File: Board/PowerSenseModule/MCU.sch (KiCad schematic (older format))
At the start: 29 parts, among them J3 Programming Header, J4 Conn_01x02_Male, U2 NCV2007x, U3 dsPIC33EV32GM102, U4 MCP2542FDxMF

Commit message: Moses's changes, removed MPLAB proj
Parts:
- added D3, D4: LED, Resistor_SMD:R_0603_1608Metric_Pad1.05x0.95mm_HandSolder, symbol Device:LED
- added R20, R21: 300, Resistor_SMD:R_0603_1608Metric_Pad1.05x0.95mm_HandSolder, symbol Device:R_US
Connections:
- net labels removed: +3.3V
- wire segments 122 -> 159
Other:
- note added: "Green"
- note added: "Red\n"
- moved on the sheet: C12

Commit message: BASE/REFERENCE
Initial Design.
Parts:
- J4: footprint Connector_PinHeader_2.54mm:PinHeader_1x02_P2.54mm_Vertical_SMD_Pin1Left -> Connector_PinHeader_2.54mm:PinHeader_1x02_P2.54mm_Vertical
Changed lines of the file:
@@
 F 0 "J4" H 1008 6206 50  0000 C CNN
 F 1 "Conn_01x02_Male" H 1008 6115 50  0000 C CNN
-F 2 "Connector_PinHeader_2.54mm:PinHeader_1x02_P2.54mm_Vertical_SMD_Pin1Left" H 900 6025 50  0001 C CNN
+F 2 "Connector_PinHeader_2.54mm:PinHeader_1x02_P2.54mm_Vertical" H 900 6025 50  0001 C CNN
 F 3 "~" H 900 6025 50  0001 C CNN
 	1    900  6025

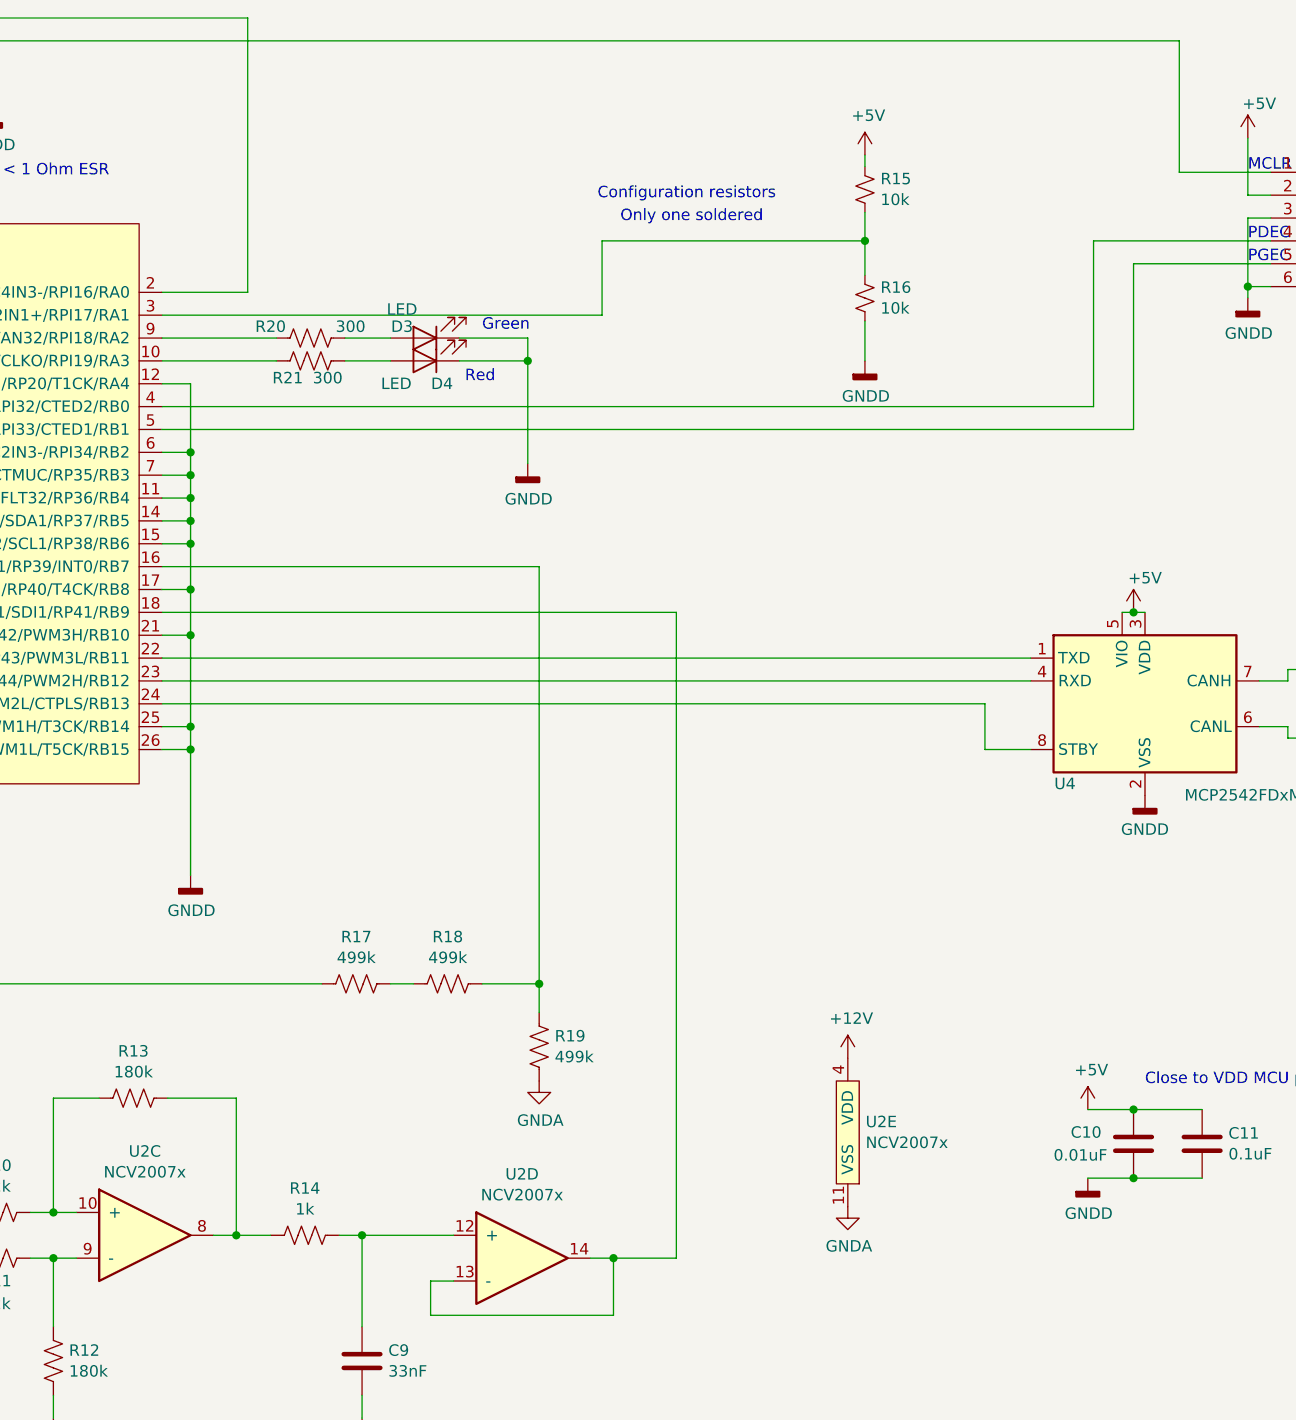
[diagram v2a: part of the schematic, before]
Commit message: Rewiring - of MCU
Rewired the MCU
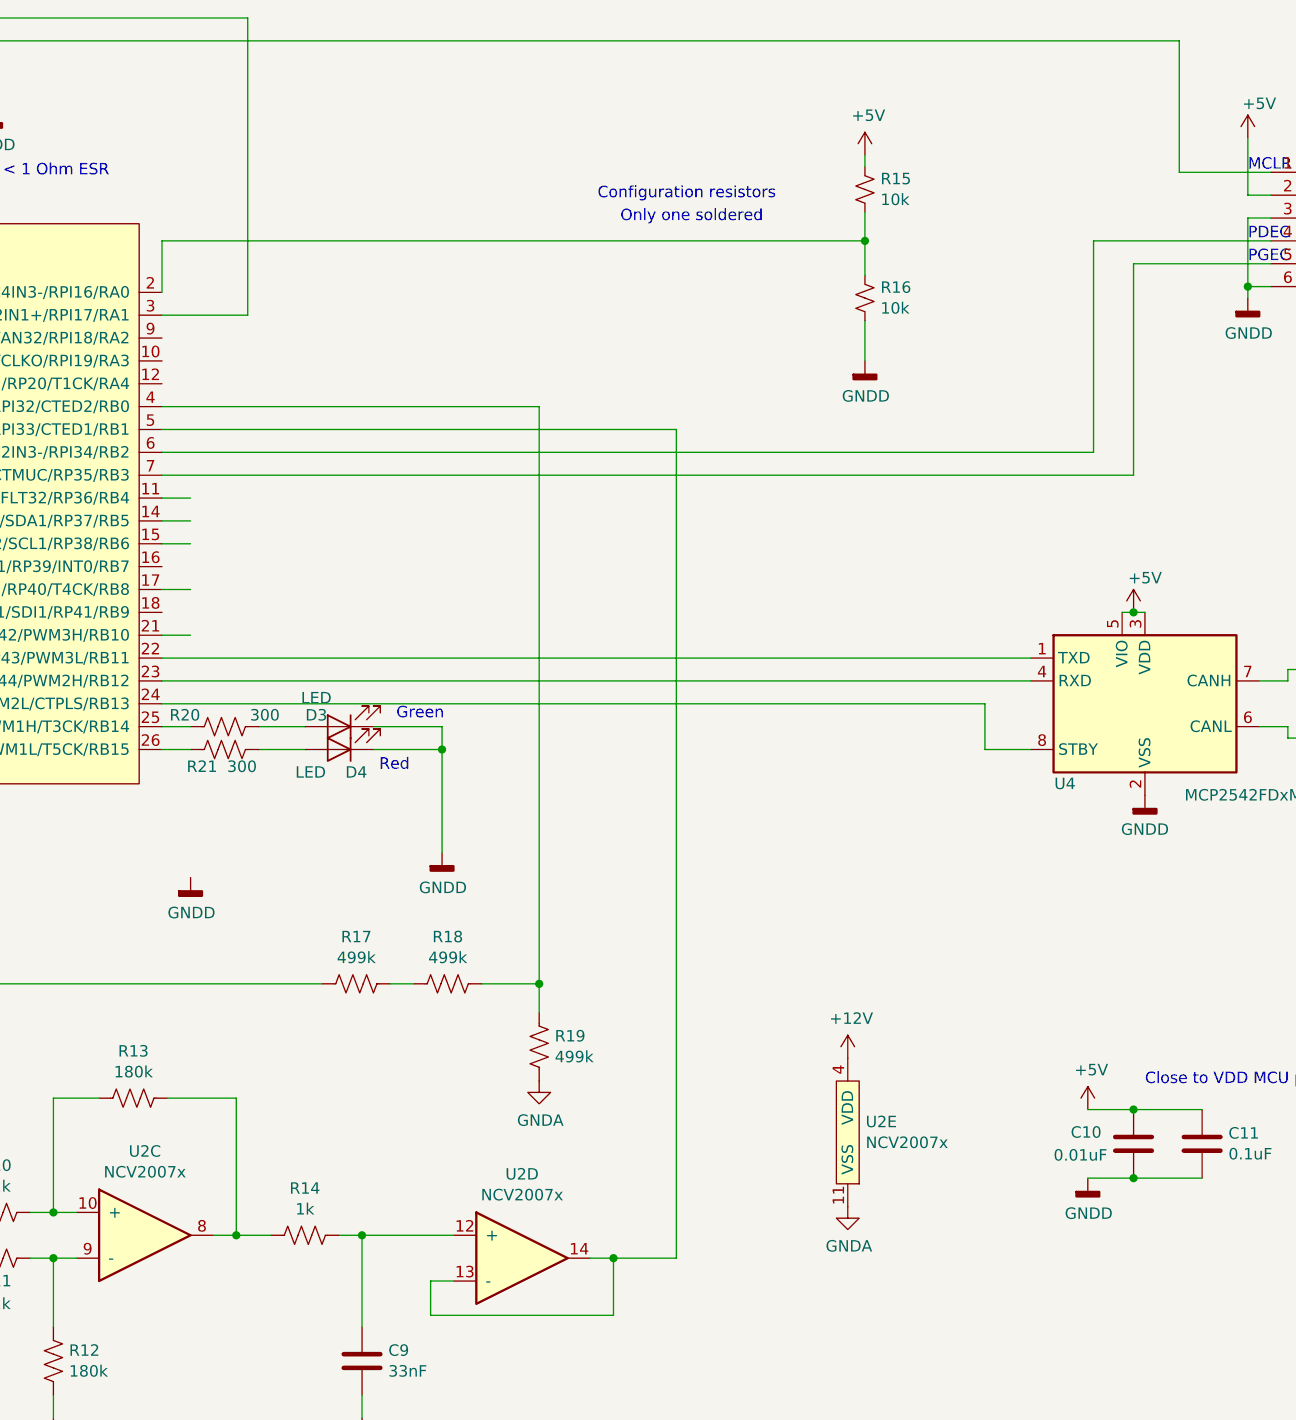
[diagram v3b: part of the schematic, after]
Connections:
- wire segments 159 -> 143
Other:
- moved on the sheet: D3, D4, R20, R21
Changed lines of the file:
@@
 $EndComp
-Wire Wire Line
-	8500 2400 8500 1675
-Wire Wire Line
-	8675 2500 8675 1775
 Wire Wire Line
 	8225 3900 8025 3900
@@
 	3300 4925 3300 5475
 Connection ~ 6075 4925
-Wire Wire Line
-	6075 3100 6075 4925
 $Comp
 L power:GNDA #PWR0101
@@
 Wire Wire Line
 	4425 3700 8025 3700
-Wire Wire Line
-	4425 2400 8500 2400
-Wire Wire Line
-	4425 2500 8675 2500
-Wire Wire Line
-	4425 3100 6075 3100
 $Comp
 L Device:C C12
@@
 $EndComp
 Wire Wire Line
-	4800 1900 4425 1900
-Wire Wire Line
-	6350 2000 4425 2000
-Wire Wire Line
-	6350 1675 6350 2000
-Wire Wire Line
 	4425 3500 8225 3500
 Wire Wire Line
 	7500 1300 7500 1350
-Wire Wire Line
-	6350 1675 7500 1675
-Wire Wire Line
-	4425 3300 6675 3300
-Wire Wire Line
-	6675 3300 6675 6125
 $Comp
 L power:GNDD #PWR0105
 U 1 1 5D4D1DB2
-P 4550 4450
-F 0 "#PWR0105" H 4550 4200 50  0001 C CNN
-F 1 "GNDD" H 4554 4295 50  0000 C CNN
-F 2 "" H 4550 4450 50  0001 C CNN
-F 3 "" H 4550 4450 50  0001 C CNN
-	1    4550 4450
-	1    0    0    -1
-$EndComp
-Wire Wire Line
-	4425 2300 4550 2300
-Wire Wire Line
-	4550 2300 4550 2600
-Wire Wire Line
-	4425 2600 4550 2600
-Connection ~ 4550 2600
-Wire Wire Line
-	4550 2600 4550 2700
-Wire Wire Line
-	4425 2700 4550 2700
-Connection ~ 4550 2700
-Wire Wire Line
-	4550 2700 4550 2800
+P 4550 4460
+F 0 "#PWR0105" H 4550 4210 50  0001 C CNN
+F 1 "GNDD" H 4554 4305 50  0000 C CNN
+F 2 "" H 4550 4460 50  0001 C CNN
+F 3 "" H 4550 4460 50  0001 C CNN
+	1    4550 4460
+	1    0    0    -1
+$EndComp
 Wire Wire Line
 	4425 2800 4550 2800
-Connection ~ 4550 2800
-Wire Wire Line
-	4550 2800 4550 2900
 Wire Wire Line
 	4425 2900 4550 2900
-Connection ~ 4550 2900
 Wire Wire Line
 	4425 3000 4550 3000
 Wire Wire Line
-	4550 2900 4550 3000
-Connection ~ 4550 3000
-Wire Wire Line
-	4550 3000 4550 3200
-Wire Wire Line
 	4425 3200 4550 3200
-Connection ~ 4550 3200
-Wire Wire Line
-	4550 3200 4550 3400
 Wire Wire Line
 	4425 3400 4550 3400
-Connection ~ 4550 3400
-Wire Wire Line
-	4550 3400 4550 3800
 Wire Wire Line
 	4425 3800 4550 3800
-Connection ~ 4550 3800
-Wire Wire Line
-	4550 3800 4550 3900
 Wire Wire Line
 	4425 3900 4550 3900
-Connection ~ 4550 3900
-Wire Wire Line
-	4550 3900 4550 4450
 $Comp
 L Device:LED D4
 U 1 1 5D518286
-P 5575 2200
-F 0 "D4" H 5500 2300 50  0000 C CNN
-F 1 "LED" H 5700 2300 50  0000 C CNN
-F 2 "Resistor_SMD:R_0603_1608Metric_Pad1.05x0.95mm_HandSolder" H 5575 2200 50  0001 C CNN
-F 3 "~" H 5575 2200 50  0001 C CNN
-	1    5575 2200
+P 5200 3900
+F 0 "D4" H 5125 4000 50  0000 C CNN
+F 1 "LED" H 5325 4000 50  0000 C CNN
+F 2 "Resistor_SMD:R_0603_1608Metric_Pad1.05x0.95mm_HandSolder" H 5200 3900 50  0001 C CNN
+F 3 "~" H 5200 3900 50  0001 C CNN
+	1    5200 3900
 	-1   0    0    1
 $EndComp
@@
 L Device:LED D3
 U 1 1 5D518C5C
-P 5575 2100
-F 0 "D3" H 5675 2050 50  0000 C CNN
-F 1 "LED" H 5675 1975 50  0000 C CNN
-F 2 "Resistor_SMD:R_0603_1608Metric_Pad1.05x0.95mm_HandSolder" H 5575 2100 50  0001 C CNN
-F 3 "~" H 5575 2100 50  0001 C CNN
-	1    5575 2100
+P 5200 3800
+F 0 "D3" H 5300 3750 50  0000 C CNN
+F 1 "LED" H 5300 3675 50  0000 C CNN
+F 2 "Resistor_SMD:R_0603_1608Metric_Pad1.05x0.95mm_HandSolder" H 5200 3800 50  0001 C CNN
+F 3 "~" H 5200 3800 50  0001 C CNN
+	1    5200 3800
 	-1   0    0    1
 $EndComp
@@
 L Device:R_US R20
 U 1 1 5D526340
-P 5075 2100
-F 0 "R20" V 5025 1925 50  0000 C CNN
-F 1 "300" V 5025 2275 50  0000 C CNN
-F 2 "Resistor_SMD:R_0603_1608Metric_Pad1.05x0.95mm_HandSolder" V 5115 2090 50  0001 C CNN
-F 3 "~" H 5075 2100 50  0001 C CNN
-	1    5075 2100
+P 4700 3800
+F 0 "R20" V 4650 3625 50  0000 C CNN
+F 1 "300" V 4650 3975 50  0000 C CNN
+F 2 "Resistor_SMD:R_0603_1608Metric_Pad1.05x0.95mm_HandSolder" V 4740 3790 50  0001 C CNN
+F 3 "~" H 4700 3800 50  0001 C CNN
+	1    4700 3800
 	0    1    1    0
 $EndComp
@@
 L Device:R_US R21
 U 1 1 5D527256
-P 5075 2200
-F 0 "R21" V 5150 2100 50  0000 C CNN
-F 1 "300" V 5150 2275 50  0000 C CNN
-F 2 "Resistor_SMD:R_0603_1608Metric_Pad1.05x0.95mm_HandSolder" V 5115 2190 50  0001 C CNN
-F 3 "~" H 5075 2200 50  0001 C CNN
-	1    5075 2200
-	0    1    1    0
-$EndComp
-Wire Wire Line
-	4425 2100 4925 2100
-Wire Wire Line
-	4925 2200 4425 2200
-Wire Wire Line
-	5425 2200 5225 2200
-Wire Wire Line
-	5425 2100 5225 2100
+P 4700 3900
+F 0 "R21" V 4775 3800 50  0000 C CNN
+F 1 "300" V 4775 3975 50  0000 C CNN
+F 2 "Resistor_SMD:R_0603_1608Metric_Pad1.05x0.95mm_HandSolder" V 4740 3890 50  0001 C CNN
+F 3 "~" H 4700 3900 50  0001 C CNN
+	1    4700 3900
+	0    1    1    0
+$EndComp
+Wire Wire Line
+	5050 3900 4850 3900
+Wire Wire Line
+	5050 3800 4850 3800
 $Comp
 L power:GNDD #PWR0106
 U 1 1 5D597A06
-P 6025 2650
-F 0 "#PWR0106" H 6025 2400 50  0001 C CNN
-F 1 "GNDD" H 6029 2495 50  0000 C CNN
-F 2 "" H 6025 2650 50  0001 C CNN
-F 3 "" H 6025 2650 50  0001 C CNN
-	1    6025 2650
-	1    0    0    -1
-$EndComp
-Wire Wire Line
-	5725 2200 6025 2200
-Wire Wire Line
-	6025 2200 6025 2650
-Wire Wire Line
-	5725 2100 6025 2100
-Wire Wire Line
-	6025 2100 6025 2200
-Connection ~ 6025 2200
-Text Notes 5825 2075 0    50   ~ 0
+P 5650 4350
+F 0 "#PWR0106" H 5650 4100 50  0001 C CNN
+F 1 "GNDD" H 5654 4195 50  0000 C CNN
+F 2 "" H 5650 4350 50  0001 C CNN
+F 3 "" H 5650 4350 50  0001 C CNN
+	1    5650 4350
+	1    0    0    -1
+$EndComp
+Wire Wire Line
+	5350 3900 5650 3900
+Wire Wire Line
+	5650 3900 5650 4350
+Wire Wire Line
+	5350 3800 5650 3800
+Wire Wire Line
+	5650 3800 5650 3900
+Connection ~ 5650 3900
+Text Notes 5450 3775 0    50   ~ 0
 Green
-Text Notes 5750 2300 0    50   ~ 0
+Text Notes 5375 4000 0    50   ~ 0
 Red\n
 Wire Wire Line
@@
 	800  700  4800 700
 Wire Wire Line
-	4800 700  4800 1900
-Wire Wire Line
 	8875 800  975  800
+Wire Wire Line
+	8500 1675 8500 2600
+Wire Wire Line
+	4425 2600 8500 2600
+Wire Wire Line
+	8675 1775 8675 2700
+Wire Wire Line
+	4425 2700 8675 2700
+Wire Wire Line
+	6075 2400 4425 2400
+Wire Wire Line
+	6075 2400 6075 4925
+Wire Wire Line
+	6675 2500 4425 2500
+Wire Wire Line
+	6675 2500 6675 6125
+Wire Wire Line
+	4800 2000 4425 2000
+Wire Wire Line
+	4800 700  4800 2000
+Wire Wire Line
+	4425 1675 4425 1900
+Wire Wire Line
+	4425 1675 7500 1675
 $EndSCHEMATC
